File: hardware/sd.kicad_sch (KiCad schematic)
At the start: 9 parts, among them J4 microSD

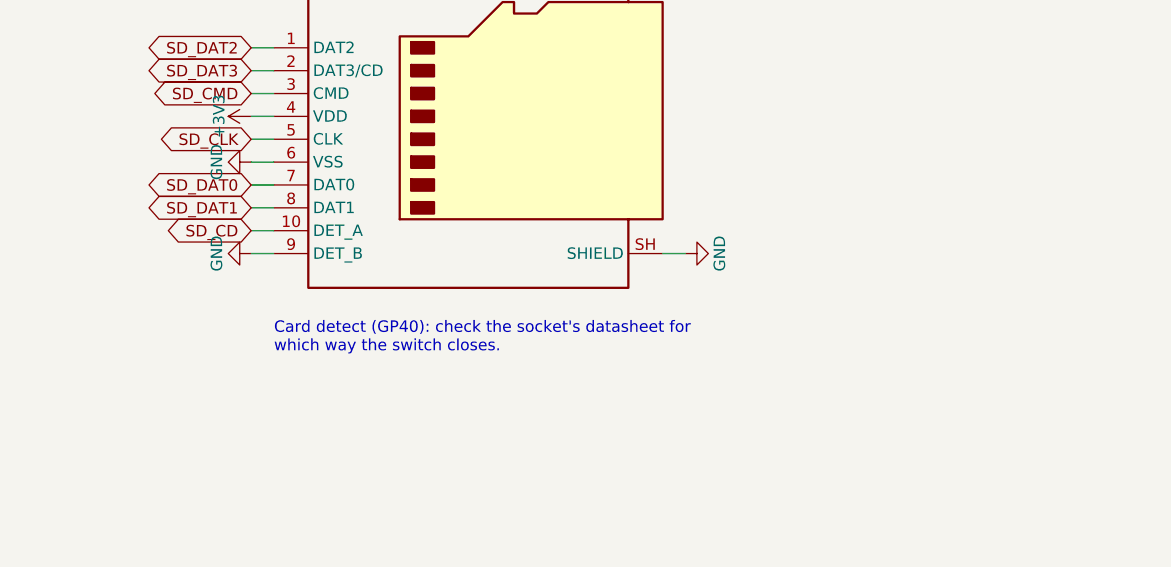
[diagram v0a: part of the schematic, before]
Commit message: PCB rev 0.2: RP2350B on the board instead of the PGA2350 module
The PGA2350 is replaced by an RP2350B with Raspberry Pi's minimal-design
support circuit: their core regulator (polarity-marked inductor), 12 MHz
crystal, W25Q128 flash and USB 27R, with their regulator, QSPI and USB
layout copied relative to the VREG_LX pin; an AMS1117 makes 3V3. GPIO
numbers are unchanged. Supply pins each have a via under the chip.

Cheaper parts from the HDD Synth Mk5: HRO TYPE-C-31-M-12 USB-C, TS-1187A
buttons, and a generic TF PUSH microSD socket. The CB3T3245 bus switches
stay. Every symbol carries its LCSC part number, and Fabrication Toolkit
offsets where JLCPCB's footprint differs from KiCad's; jlcpcb.py applies
the same fitted corrections. check_netlist.py also checks the RP2350
support circuit. ERC and DRC are clean; parts for 5 boards about $68.50.

Co-Authored-By: Claude Opus 5.5 <noreply@anthropic.com>
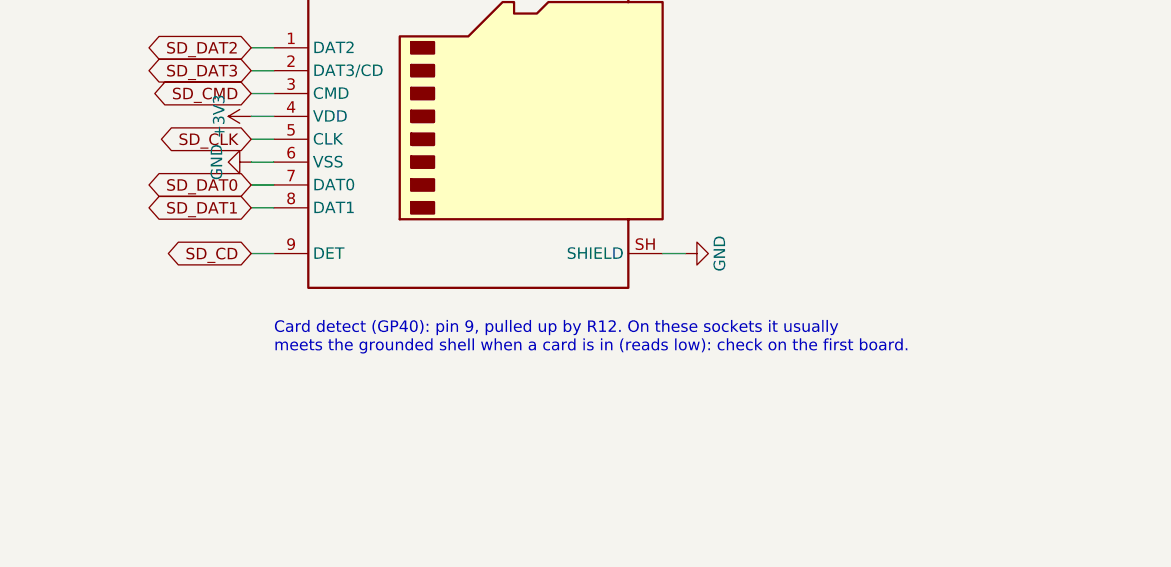
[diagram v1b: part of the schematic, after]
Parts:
- C2: LCSC (none) -> C15850
- C3: LCSC (none) -> C14663
- J4: footprint Connector_Card:microSD_HC_Hirose_DM3AT-SF-PEJM5 -> HDDSynthPro:microSD_TF-PUSH; symbol Connector:Micro_SD_Card_Det_Hirose_DM3AT -> Connector:Micro_SD_Card_Det1; FT Position Offset (none) -> 0,0.15; LCSC (none) -> C393941; MPN (none) -> TF PUSH (generic push-push)
- R10, R11, R12, R7, R8, R9: LCSC (none) -> C25804
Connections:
- net GND: no longer J4.9 (DET_B)
- net SD_CD: now also J4.9 (DET); no longer J4.10 (DET_A)
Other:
- note added: "Card detect (GP40): pin 9, pulled up by R12. On these sockets it usually meets the grounded shell when a card is in (reads low): check on the first board."
- note removed: "Card detect (GP40): check the socket's datasheet for which way the switch closes."
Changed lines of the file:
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@@
 	)
 	(symbol
-		(lib_id "Connector:Micro_SD_Card_Det_Hirose_DM3AT")
+		(lib_id "Connector:Micro_SD_Card_Det1")
 		(at 228.6 111.76 0)
 		(unit 1)
@@
 			)
 		)
-		(property "Footprint" "Connector_Card:microSD_HC_Hirose_DM3AT-SF-PEJM5"
+		(property "Footprint" "HDDSynthPro:microSD_TF-PUSH"
 			(at 280.67 93.98 0)
 			(effects
@@
 			)
 		)
-		(property "Datasheet" "https://www.hirose.com/product/en/download_file/key_name/DM3/category/Catalog/doc_file_id/49662/?file_category_id=4&item_id=195&is_series=1"
+		(property "Datasheet" "https://datasheet.lcsc.com/lcsc/2110151630_XKB-Connectivity-XKTF-015-N_C381082.pdf"
 			(at 228.6 109.22 0)
 			(effects
@@
 			)
 		)
-		(property "Description" "Micro SD Card Socket with card detection pins"
+		(property "Description" "Micro SD Card Socket with one card detection pin"
 			(at 228.6 111.76 0)
 			(effects
@@
 			)
 		)
+		(property "MPN" "TF PUSH (generic push-push)"
+			(at 228.6 111.76 0)
+			(effects
+				(font
+					(size 1.27 1.27)
+				)
+				(hide yes)
+			)
+		)
+		(property "LCSC" "C393941"
+			(at 228.6 111.76 0)
+			(effects
+				(font
+					(size 1.27 1.27)
+				)
+				(hide yes)
+			)
+		)
+		(property "FT Position Offset" "0,0.15"
+			(at 228.6 111.76 0)
+			(effects
+				(font
+					(size 1.27 1.27)
+				)
+				(hide yes)
+			)
+		)
 		(pin "1"
 		)
@@
 		)
 		(pin "9"
-		)
-		(pin "10"
 		)
 		(pin "SH"
@@
 		(on_board yes)
 		(dnp no)
-		(property "Reference" "#PWR050"
+		(property "Reference" "#PWR092"
 			(at 207.01 109.22 0)
 			(effects
@@
 			(project "hddsynthpro"
 				(path "/1f1928de-57c1-5ffb-9b24-ae415e42f504/4bb0f041-3105-5779-949a-0ee0388ac573"
-					(reference "#PWR050")
+					(reference "#PWR092")
 					(unit 1)
 				)
@@
 		(on_board yes)
 		(dnp no)
-		(property "Reference" "#PWR051"
+		(property "Reference" "#PWR093"
 			(at 196.85 114.3 0)
 			(effects
@@
 			(project "hddsynthpro"
 				(path "/1f1928de-57c1-5ffb-9b24-ae415e42f504/4bb0f041-3105-5779-949a-0ee0388ac573"
-					(reference "#PWR051")
+					(reference "#PWR093")
 					(unit 1)
 				)
@@
 		)
 	)
-	(symbol
-		(lib_id "power:GND")
-		(at 203.2 124.46 270)
-		(unit 1)
-		(exclude_from_sim no)
-		(in_bom no)
-		(on_board yes)
-		(dnp no)
-		(property "Reference" "#PWR052"
-			(at 196.85 124.46 0)
-			(effects
-				(font
-					(size 1.27 1.27)
-				)
-				(hide yes)
-			)
-		)
-		(property "Value" "GND"
-			(at 199.39 124.46 0)
-			(effects
-				(font
-					(size 1.27 1.27)
-				)
-			)
-		)
-		(property "Footprint" ""
-			(at 203.2 124.46 0)
-			(effects
-				(font
-					(size 1.27 1.27)
-				)
-				(hide yes)
-			)
-		)
-		(property "Datasheet" ""
-			(at 203.2 124.46 0)
-			(effects
-				(font
-					(size 1.27 1.27)
-				)
-				(hide yes)
-			)
-		)
-		(property "Description" "Power symbol creates a global label with name \"GND\" , ground"
-			(at 203.2 124.46 0)
-			(effects
-				(font
-					(size 1.27 1.27)
-				)
-				(hide yes)
-			)
-		)
-		(pin "1"
-		)
-		(instances
-			(project "hddsynthpro"
-				(path "/1f1928de-57c1-5ffb-9b24-ae415e42f504/4bb0f041-3105-5779-949a-0ee0388ac573"
-					(reference "#PWR052")
-					(unit 1)
-				)
-			)
-		)
-	)
-	(wire
-		(pts
-			(xy 205.74 121.92)
-			(xy 203.2 121.92)
-		)
-		(stroke
-			(width 0)
-			(type default)
-		)
-	)
 	(wire
 		(pts
@@
 		(on_board yes)
 		(dnp no)
-		(property "Reference" "#PWR053"
+		(property "Reference" "#PWR094"
 			(at 257.81 124.46 0)
 			(effects
@@
 			(project "hddsynthpro"
 				(path "/1f1928de-57c1-5ffb-9b24-ae415e42f504/4bb0f041-3105-5779-949a-0ee0388ac573"
-					(reference "#PWR053")
-					(unit 1)
-				)
-			)
-		)
-	)
-	(text "Card detect (GP40): check the socket's datasheet for\nwhich way the switch closes."
+					(reference "#PWR094")
+					(unit 1)
+				)
+			)
+		)
+	)
+	(text "Card detect (GP40): pin 9, pulled up by R12. On these sockets it usually\nmeets the grounded shell when a card is in (reads low): check on the first board."
 		(exclude_from_sim no)
 		(at 205.74 132.08 0)
@@
 			)
 		)
+		(property "LCSC" "C25804"
+			(at 63.5 99.06 0)
+			(effects
+				(font
+					(size 1.27 1.27)
+				)
+				(hide yes)
+			)
+		)
 		(pin "1"
 		)
@@
 		(on_board yes)
 		(dnp no)
-		(property "Reference" "#PWR054"
+		(property "Reference" "#PWR095"
 			(at 63.5 96.52 0)
 			(effects
@@
 			(project "hddsynthpro"
 				(path "/1f1928de-57c1-5ffb-9b24-ae415e42f504/4bb0f041-3105-5779-949a-0ee0388ac573"
-					(reference "#PWR054")
+					(reference "#PWR095")
 					(unit 1)
 				)
@@
 			)
 		)
+		(property "LCSC" "C25804"
+			(at 81.28 99.06 0)
+			(effects
+				(font
+					(size 1.27 1.27)
+				)
+				(hide yes)
+			)
+		)
 		(pin "1"
 		)
@@
 		(on_board yes)
 		(dnp no)
-		(property "Reference" "#PWR055"
+		(property "Reference" "#PWR096"
 			(at 81.28 96.52 0)
 			(effects
@@
 			(project "hddsynthpro"
 				(path "/1f1928de-57c1-5ffb-9b24-ae415e42f504/4bb0f041-3105-5779-949a-0ee0388ac573"
-					(reference "#PWR055")
+					(reference "#PWR096")
 					(unit 1)
 				)
@@
 			)
 		)
+		(property "LCSC" "C25804"
+			(at 99.06 99.06 0)
+			(effects
+				(font
+					(size 1.27 1.27)
+				)
+				(hide yes)
+			)
+		)
 		(pin "1"
 		)
@@
 		(on_board yes)
 		(dnp no)
-		(property "Reference" "#PWR056"
+		(property "Reference" "#PWR097"
 			(at 99.06 96.52 0)
 			(effects
@@
 			(project "hddsynthpro"
 				(path "/1f1928de-57c1-5ffb-9b24-ae415e42f504/4bb0f041-3105-5779-949a-0ee0388ac573"
-					(reference "#PWR056")
+					(reference "#PWR097")
 					(unit 1)
 				)
@@
 			)
 		)
+		(property "LCSC" "C25804"
+			(at 116.84 99.06 0)
+			(effects
+				(font
+					(size 1.27 1.27)
+				)
+				(hide yes)
+			)
+		)
 		(pin "1"
 		)
@@
 		(on_board yes)
 		(dnp no)
-		(property "Reference" "#PWR057"
+		(property "Reference" "#PWR098"
 			(at 116.84 96.52 0)
 			(effects
@@
 			(project "hddsynthpro"
 				(path "/1f1928de-57c1-5ffb-9b24-ae415e42f504/4bb0f041-3105-5779-949a-0ee0388ac573"
-					(reference "#PWR057")
+					(reference "#PWR098")
 					(unit 1)
 				)
@@
 			)
 		)
+		(property "LCSC" "C25804"
+			(at 134.62 99.06 0)
+			(effects
+				(font
+					(size 1.27 1.27)
+				)
+				(hide yes)
+			)
+		)
 		(pin "1"
 		)
@@
 		(on_board yes)
 		(dnp no)
-		(property "Reference" "#PWR058"
+		(property "Reference" "#PWR099"
 			(at 134.62 96.52 0)
 			(effects
@@
 			(project "hddsynthpro"
 				(path "/1f1928de-57c1-5ffb-9b24-ae415e42f504/4bb0f041-3105-5779-949a-0ee0388ac573"
-					(reference "#PWR058")
+					(reference "#PWR099")
 					(unit 1)
 				)
@@
 			)
 		)
+		(property "LCSC" "C25804"
+			(at 152.4 99.06 0)
+			(effects
+				(font
+					(size 1.27 1.27)
+				)
+				(hide yes)
+			)
+		)
 		(pin "1"
 		)
@@
 		(on_board yes)
 		(dnp no)
-		(property "Reference" "#PWR059"
+		(property "Reference" "#PWR100"
 			(at 152.4 96.52 0)
 			(effects
@@
 			(project "hddsynthpro"
 				(path "/1f1928de-57c1-5ffb-9b24-ae415e42f504/4bb0f041-3105-5779-949a-0ee0388ac573"
-					(reference "#PWR059")
+					(reference "#PWR100")
 					(unit 1)
 				)
@@
 			)
 		)
+		(property "LCSC" "C15850"
+			(at 81.28 149.86 0)
+			(effects
+				(font
+					(size 1.27 1.27)
+				)
+				(hide yes)
+			)
+		)
 		(pin "1"
 		)
@@
 		(on_board yes)
 		(dnp no)
-		(property "Reference" "#PWR060"
+		(property "Reference" "#PWR101"
 			(at 81.28 147.32 0)
 			(effects
@@
 			(project "hddsynthpro"
 				(path "/1f1928de-57c1-5ffb-9b24-ae415e42f504/4bb0f041-3105-5779-949a-0ee0388ac573"
-					(reference "#PWR060")
+					(reference "#PWR101")
 					(unit 1)
 				)
@@
 		(on_board yes)
 		(dnp no)
-		(property "Reference" "#PWR061"
+		(property "Reference" "#PWR102"
 			(at 81.28 162.56 0)
 			(effects
@@
 			(project "hddsynthpro"
 				(path "/1f1928de-57c1-5ffb-9b24-ae415e42f504/4bb0f041-3105-5779-949a-0ee0388ac573"
-					(reference "#PWR061")
+					(reference "#PWR102")
 					(unit 1)
 				)
@@
 			)
 		)
+		(property "LCSC" "C14663"
+			(at 99.06 149.86 0)
+			(effects
+				(font
+					(size 1.27 1.27)
+				)
+				(hide yes)
+			)
+		)
 		(pin "1"
 		)
@@
 		(on_board yes)
 		(dnp no)
-		(property "Reference" "#PWR062"
+		(property "Reference" "#PWR103"
 			(at 99.06 147.32 0)
 			(effects
@@
 			(project "hddsynthpro"
 				(path "/1f1928de-57c1-5ffb-9b24-ae415e42f504/4bb0f041-3105-5779-949a-0ee0388ac573"
-					(reference "#PWR062")
+					(reference "#PWR103")
 					(unit 1)
 				)
@@
 		(on_board yes)
 		(dnp no)
-		(property "Reference" "#PWR063"
+		(property "Reference" "#PWR104"
 			(at 99.06 162.56 0)
 			(effects
@@
 			(project "hddsynthpro"
 				(path "/1f1928de-57c1-5ffb-9b24-ae415e42f504/4bb0f041-3105-5779-949a-0ee0388ac573"
-					(reference "#PWR063")
+					(reference "#PWR104")
 					(unit 1)
 				)
@@
 	(global_label "SD_CD"
 		(shape bidirectional)
-		(at 203.2 121.92 180)
+		(at 203.2 124.46 180)
 		(fields_autoplaced yes)
 		(effects
@@
 		)
 		(property "Intersheetrefs" "${INTERSHEET_REFS}"
-			(at 203.2 121.92 180)
-			(effects
-				(font
+			(at 203.2 124.46 180)
+			(effects
+				(font
